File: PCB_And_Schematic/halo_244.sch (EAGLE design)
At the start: 12 parts

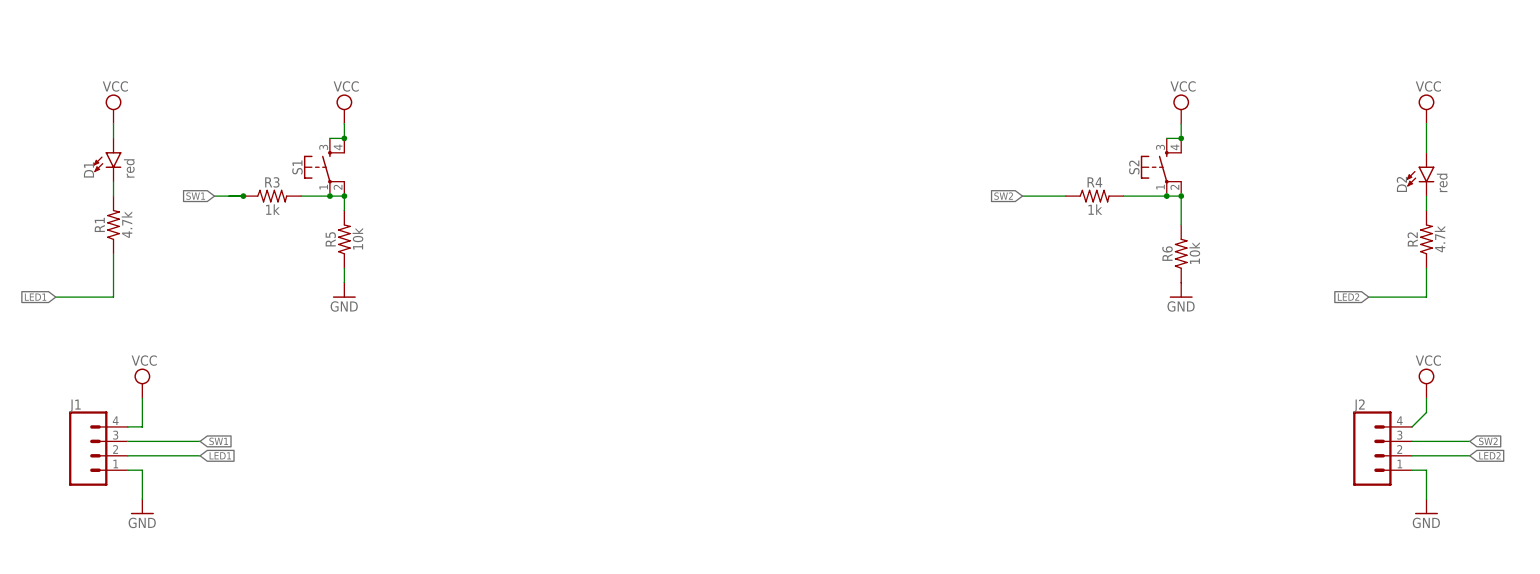
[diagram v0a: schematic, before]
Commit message: reduced the size of board
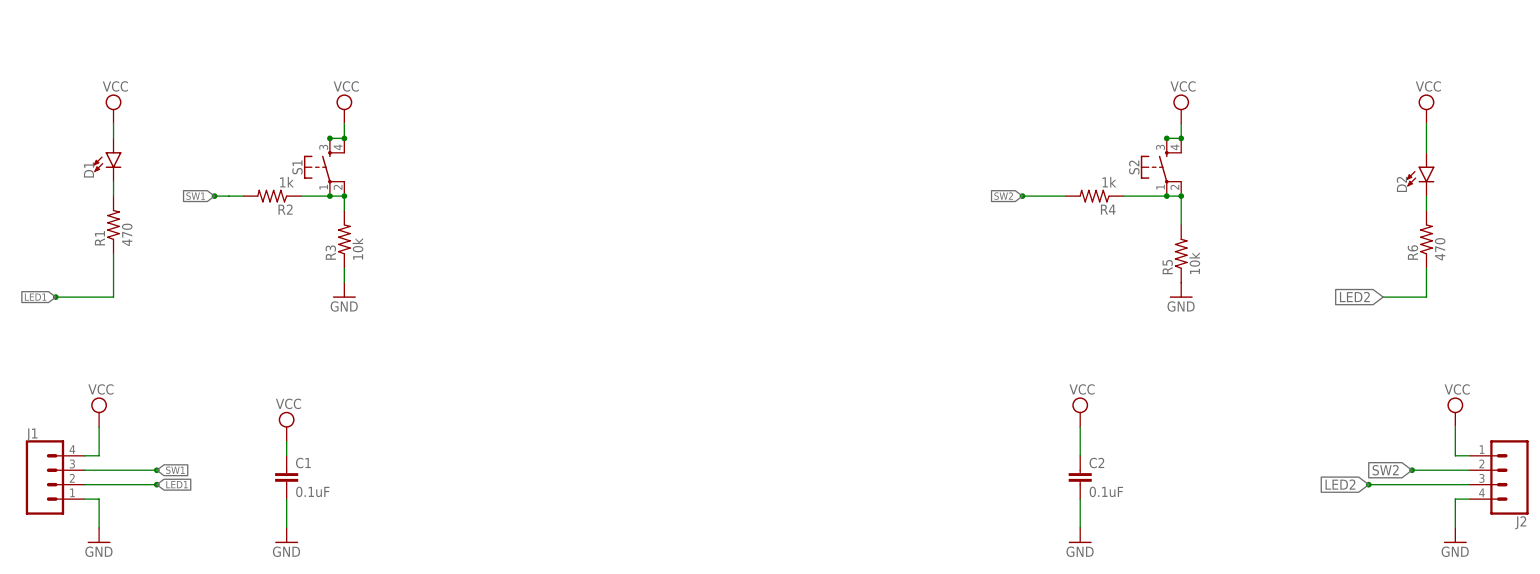
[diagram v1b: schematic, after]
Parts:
- added C1, C2: 0.1uF, SparkFun-Capacitors:0.1UF-KIT-EZ-50V-20%
- D1, D2: value red -> (none); device SparkFun-LED:LED5MM -> SparkFun-LED:LED-3MM-NO_SILK
- J1, J2: OC_NEWARK (none) -> unknown
- R1: value 4.7k -> 470; device SparkFun-Resistors:4.7KOHM-0603-1/10W-1% -> rcl:R-US_0207/12; MF (none) -> FARNELL; MPN (none) -> MCF 0.25W 470R; OC_NEWARK (none) -> 38K0375
- R2: value 4.7k -> 1k; device SparkFun-Resistors:4.7KOHM-0603-1/10W-1% -> rcl:R-US_0207/12; OC_NEWARK (none) -> unknown
- R3: value 1k -> 10k; device SparkFun-Resistors:1KOHM-0603-1/10W-1% -> rcl:R-US_0207/12; MF (none) -> FARNELL; MPN (none) -> MCF 0.25W 10K; OC_NEWARK (none) -> 38K0328
- R4: device SparkFun-Resistors:1KOHM-0603-1/10W-1% -> rcl:R-US_0207/12; OC_NEWARK (none) -> unknown
- R5: device SparkFun-Resistors:10KOHM-0603-1/10W-1% -> rcl:R-US_0207/12; MF (none) -> FARNELL; MPN (none) -> MCF 0.25W 10K; OC_NEWARK (none) -> 38K0328
- R6: value 10k -> 470; device SparkFun-Resistors:10KOHM-0603-1/10W-1% -> rcl:R-US_0207/12; MF (none) -> FARNELL; MPN (none) -> MCF 0.25W 470R; OC_NEWARK (none) -> 38K0375
- S1, S2: MF (none) -> TYCO ELECTRONICS; MPN (none) -> FSM2JSMAATR; OC_NEWARK (none) -> 14H0922
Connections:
- net GND: now also C1.2, C2.2, J2.4, R3.1; no longer J2.1, R6.1
- net LED2: now also J2.3, R6.1; no longer J2.2, R2.1
- net N$1: now also R2.1; no longer R5.2
- net N$3: now also R6.2; no longer R2.2
- net N$4: now also R4.1, R5.2; no longer R4.2, R6.2
- net SW1: now also R2.2; no longer R3.1
- net SW2: now also J2.2, R4.2; no longer J2.3, R4.1
- net VCC: now also C1.1, C2.1, J2.1; no longer J2.4
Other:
- moved on the sheet: J1, J2, R2, R3, R4, R5, R6

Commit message: final pcb files
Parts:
- S1, S2: value (none) -> MOMENTARY-SWITCH-SPST-PTH-6.0MM; device SparkFun-Switches:MOMENTARY-SWITCH-SPST-2-SMD-4.6X2.8MM -> SparkFun-Switches:MOMENTARY-SWITCH-SPST-PTH-6.0MM; MF TYCO ELECTRONICS -> (none); MPN FSM2JSMAATR -> (none); OC_NEWARK 14H0922 -> (none)
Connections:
- net N$1: no longer S1.2
- net N$4: no longer S2.2
- net VCC: now also S1.2, S2.2; no longer S1.3, S1.4, S2.3, S2.4
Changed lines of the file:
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@@
 <setting verticaltext="up"/>
 </settings>
-<grid distance="0.1" unitdist="inch" unit="mil" style="lines" multiple="1" display="yes" altdistance="0.01" altunitdist="inch" altunit="mil"/>
+<grid distance="0.1" unitdist="inch" unit="inch" style="lines" multiple="1" display="no" altdistance="0.01" altunitdist="inch" altunit="inch"/>
 <layers>
 <layer number="1" name="Top" color="4" fill="1" visible="no" active="no"/>
@@
 <attribute name="OC_NEWARK" value="unknown"/>
 </part>
-<part name="S1" library="SparkFun-Switches" deviceset="MOMENTARY-SWITCH-SPST-2" device="-SMD-4.6X2.8MM">
-<attribute name="MF" value="TYCO ELECTRONICS"/>
-<attribute name="MPN" value="FSM2JSMAATR"/>
-<attribute name="OC_NEWARK" value="14H0922"/>
-</part>
-<part name="S2" library="SparkFun-Switches" deviceset="MOMENTARY-SWITCH-SPST-2" device="-SMD-4.6X2.8MM">
-<attribute name="MF" value="TYCO ELECTRONICS"/>
-<attribute name="MPN" value="FSM2JSMAATR"/>
-<attribute name="OC_NEWARK" value="14H0922"/>
-</part>
 <part name="SUPPLY1" library="supply2" deviceset="VCC" device=""/>
 <part name="SUPPLY2" library="supply2" deviceset="VCC" device=""/>
@@
 <part name="GND2" library="supply1" deviceset="GND" device=""/>
 <part name="GND3" library="supply1" deviceset="GND" device=""/>
+<part name="S1" library="SparkFun-Switches" deviceset="MOMENTARY-SWITCH-SPST" device="-PTH-6.0MM" value="MOMENTARY-SWITCH-SPST-PTH-6.0MM"/>
+<part name="S2" library="SparkFun-Switches" deviceset="MOMENTARY-SWITCH-SPST" device="-PTH-6.0MM" value="MOMENTARY-SWITCH-SPST-PTH-6.0MM"/>
 </parts>
 <sheets>
@@
 <attribute name="MF" x="266.7" y="101.6" size="1.778" layer="96" display="off"/>
 <attribute name="MPN" x="266.7" y="101.6" size="1.778" layer="96" display="off"/>
-</instance>
-<instance part="S1" gate="G$1" x="60.96" y="154.94" rot="R90">
-<attribute name="OC_NEWARK" x="60.96" y="154.94" size="1.778" layer="96" rot="R180" display="off"/>
-<attribute name="MF" x="60.96" y="154.94" size="1.778" layer="96" rot="R180" display="off"/>
-<attribute name="MPN" x="60.96" y="154.94" size="1.778" layer="96" rot="R180" display="off"/>
-</instance>
-<instance part="S2" gate="G$1" x="208.28" y="154.94" rot="R90">
-<attribute name="OC_NEWARK" x="208.28" y="154.94" size="1.778" layer="96" rot="R180" display="off"/>
-<attribute name="MF" x="208.28" y="154.94" size="1.778" layer="96" rot="R180" display="off"/>
-<attribute name="MPN" x="208.28" y="154.94" size="1.778" layer="96" rot="R180" display="off"/>
 </instance>
 <instance part="SUPPLY1" gate="G$1" x="63.5" y="165.1"/>
@@
 <instance part="GND2" gate="1" x="53.34" y="88.9"/>
 <instance part="GND3" gate="1" x="193.04" y="88.9"/>
+<instance part="S1" gate="G$1" x="63.5" y="154.94" rot="R90"/>
+<instance part="S2" gate="G$1" x="210.82" y="154.94" rot="R90"/>
 </instances>
 <busses>
@@
 <segment>
 <pinref part="SUPPLY1" gate="G$1" pin="VCC"/>
-<pinref part="S1" gate="G$1" pin="4"/>
-<pinref part="S1" gate="G$1" pin="3"/>
-<wire x1="60.96" y1="160.02" x2="63.5" y2="160.02" width="0.1524" layer="91"/>
-<junction x="63.5" y="160.02"/>
 <wire x1="63.5" y1="160.02" x2="63.5" y2="162.56" width="0.1524" layer="91"/>
-<junction x="60.96" y="160.02"/>
-</segment>
-<segment>
-<pinref part="S2" gate="G$1" pin="4"/>
+<pinref part="S1" gate="G$1" pin="2"/>
+</segment>
+<segment>
 <pinref part="SUPPLY2" gate="G$1" pin="VCC"/>
 <wire x1="210.82" y1="160.02" x2="210.82" y2="162.56" width="0.1524" layer="91"/>
-<pinref part="S2" gate="G$1" pin="3"/>
-<wire x1="208.28" y1="160.02" x2="210.82" y2="160.02" width="0.1524" layer="91"/>
-<junction x="210.82" y="160.02"/>
-<junction x="208.28" y="160.02"/>
+<pinref part="S2" gate="G$1" pin="2"/>
 </segment>
 <segment>
@@
 <net name="N$1" class="0">
 <segment>
-<pinref part="S1" gate="G$1" pin="2"/>
 <wire x1="63.5" y1="149.86" x2="63.5" y2="147.32" width="0.1524" layer="91"/>
-<wire x1="55.88" y1="149.86" x2="60.96" y2="149.86" width="0.1524" layer="91"/>
+<pinref part="R3" gate="G$1" pin="2"/>
+<pinref part="S1" gate="G$1" pin="1"/>
+<pinref part="R2" gate="G$1" pin="1"/>
+<wire x1="55.88" y1="149.86" x2="63.5" y2="149.86" width="0.1524" layer="91"/>
 <junction x="63.5" y="149.86"/>
-<pinref part="S1" gate="G$1" pin="1"/>
-<wire x1="60.96" y1="149.86" x2="63.5" y2="149.86" width="0.1524" layer="91"/>
-<junction x="60.96" y="149.86"/>
-<pinref part="R3" gate="G$1" pin="2"/>
-<pinref part="R2" gate="G$1" pin="1"/>
 </segment>
 </net>
 <net name="N$4" class="0">
 <segment>
-<pinref part="S2" gate="G$1" pin="2"/>
-<wire x1="200.66" y1="149.86" x2="208.28" y2="149.86" width="0.1524" layer="91"/>
-<wire x1="208.28" y1="149.86" x2="210.82" y2="149.86" width="0.1524" layer="91"/>
 <wire x1="210.82" y1="144.78" x2="210.82" y2="149.86" width="0.1524" layer="91"/>
+<pinref part="R5" gate="G$1" pin="2"/>
+<pinref part="S2" gate="G$1" pin="1"/>
+<pinref part="R4" gate="G$1" pin="1"/>
+<wire x1="200.66" y1="149.86" x2="210.82" y2="149.86" width="0.1524" layer="91"/>
 <junction x="210.82" y="149.86"/>
-<pinref part="S2" gate="G$1" pin="1"/>
-<junction x="208.28" y="149.86"/>
-<pinref part="R5" gate="G$1" pin="2"/>
-<pinref part="R4" gate="G$1" pin="1"/>
-</segment>
-</net>
+</segment>
+</net>
